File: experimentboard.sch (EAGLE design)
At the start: 72 parts, among them IC1 TL072P, IC2 LM317, IC3 LM337, Q1 27 MHz, U1 PCM1690, U2 PLL1706

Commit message: Taking the Beaglebone approach
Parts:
- removed C16, C17, C18: 100 nF ml, rcl:C-EU050-024X044
- removed Q1: 27 MHz, special:XTAL/S
- removed R2: 22, rcl:R-EU_0207/7
- removed SV1: (no value), 0000halfgaar:RASPBERRYPI2
- added JP1, JP2: (no value), jumper:JP2Q
- added R15: 680, rcl:R-EU_0207/7
- added R27: 0, rcl:R-EU_0207/10
- added R30, R31, R32, R33, R35, R36, R37: 22, rcl:R-EU_0207/7
- added R38, R39: 5.6k, rcl:R-EU_0207/7
- added U$2: BEAGLEBONEP9, 0000halfgaar:BEAGLEBONEP9
- C1: value 22pf -> 4.7n
- C15: value 100 nF ml -> 1µF ml
- C2: value 22pf -> 68n
- R1: value 22 -> 0; device rcl:R-EU_0207/7 -> rcl:R-EU_0207/10
- R23, R24: value 2.7k -> 715
- R3: value 22 -> 10k
- U2: value PLL1706 -> DIR9001; device 0000halfgaar:PLL1705 -> 0000halfgaar:DIR9001
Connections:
- removed net MOSI: SV1.GPIO10/MOSI, U1.MD/SDA/DEMP, U2.FS1/MD
- removed net N$10: R1.1, SV1.GPIO19/LRCK
- removed net N$9: R2.1, SV1.GPIO18/BCK
- removed net SCKL: SV1.GPIO11/SCLK, U1.MC/SCL/FMT, U2.FS2/MC
- removed net U1SEL: SV1.GPIO22, U1.MS/ADR0/RSV
- removed net U2SEL: SV1.GPIO15, U2.SR/ML
- new net ACLKR: R31.1, U$2.ACLKR
- new net ACLKX: R36.1, U$2.ACLKX
- new net AHCLKX: R35.1, U$2.FSX
- new net DIN: R32.1, U$2.DIN
- new net DIR_AUDIO: U$2.DIR_AUDIO(GPIO1_19), U2.AUDIO
- new net DOUT: R37.1, U$2.DOUT
- new net FSR: R30.1, U$2.FSR
- new net MCLK: R4.1, U$2.AHCLKX
- new net N$20: U2.RXIN
- new net N$51: R32.2, U2.DOUT
- new net N$52: R31.2, U2.BCKO
- new net N$53: R30.2, U2.LRCKO
- new net N$54: R33.2, U2.SCKO
- new net N$61: R37.2, U1.DIN1
- new net N$62: R36.2, U1.BCK
- new net N$63: R35.2, U1.LRCK
- new net RST: U$2.RESET(GPIO1_16), U1.RST, U2.RST
- new net SCL: R38.1, U$2.I2C_SCL, U1.MC/SCL/FMT
- new net SDA: R39.1, U$2.I2C_SDA, U1.MD/SDA/DEMP
- net AGND: now also C1.1, C2.1, R1.2; no longer C16.1
- net DGND: now also C15.2, R1.1, R7.1, U$2.DGND, U2.DGND, U2.RSV, U2.XTI; no longer C1.1, C15.1, C17.1, C18.2, C2.1, SV1.GND@1, U2.DGND1, U2.DGND2, U2.DGND3
- net N$1: now also JP2.3, U2.PSCK1; no longer R1.2, U1.LRCK
- net N$2: now also R3.2, U1.TEST/ADR1/RSV; no longer R2.2, U1.BCK
- net N$3: now also JP2.1, U2.PSCK0; no longer R3.2, U1.DIN1
- net N$4: now also C1.2, R15.1, U2.FILT; no longer R4.1, U2.SCKO3
- net N$6: now also C2.2, R15.2; no longer C1.2, Q1.2, U2.XT1
- net N$7: now also JP1.4, U2.FMT0; no longer C2.2, Q1.1, U2.XT2
- net N$8: now also JP1.2, U2.FMT1; no longer R3.1, SV1.GPIO21/I2SOUT
- net V+: now also R27.2
- net VCC: now also R27.1, U$2.VDD_5V; no longer C16.2
- net VDD: now also C15.1, JP1.1, JP1.3, JP2.2, JP2.4, R3.1, R38.2, R39.2, U$2.3.3V, U2.VDD; no longer C15.2, C17.2, C18.1, R7.1, SV1.3V3@1, SV1.3V3@2, U1.RST, U2.VDD1, U2.VDD2, U2.VDD3
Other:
- moved on the sheet: C1, C15, C2, C32, R1, R3, R4

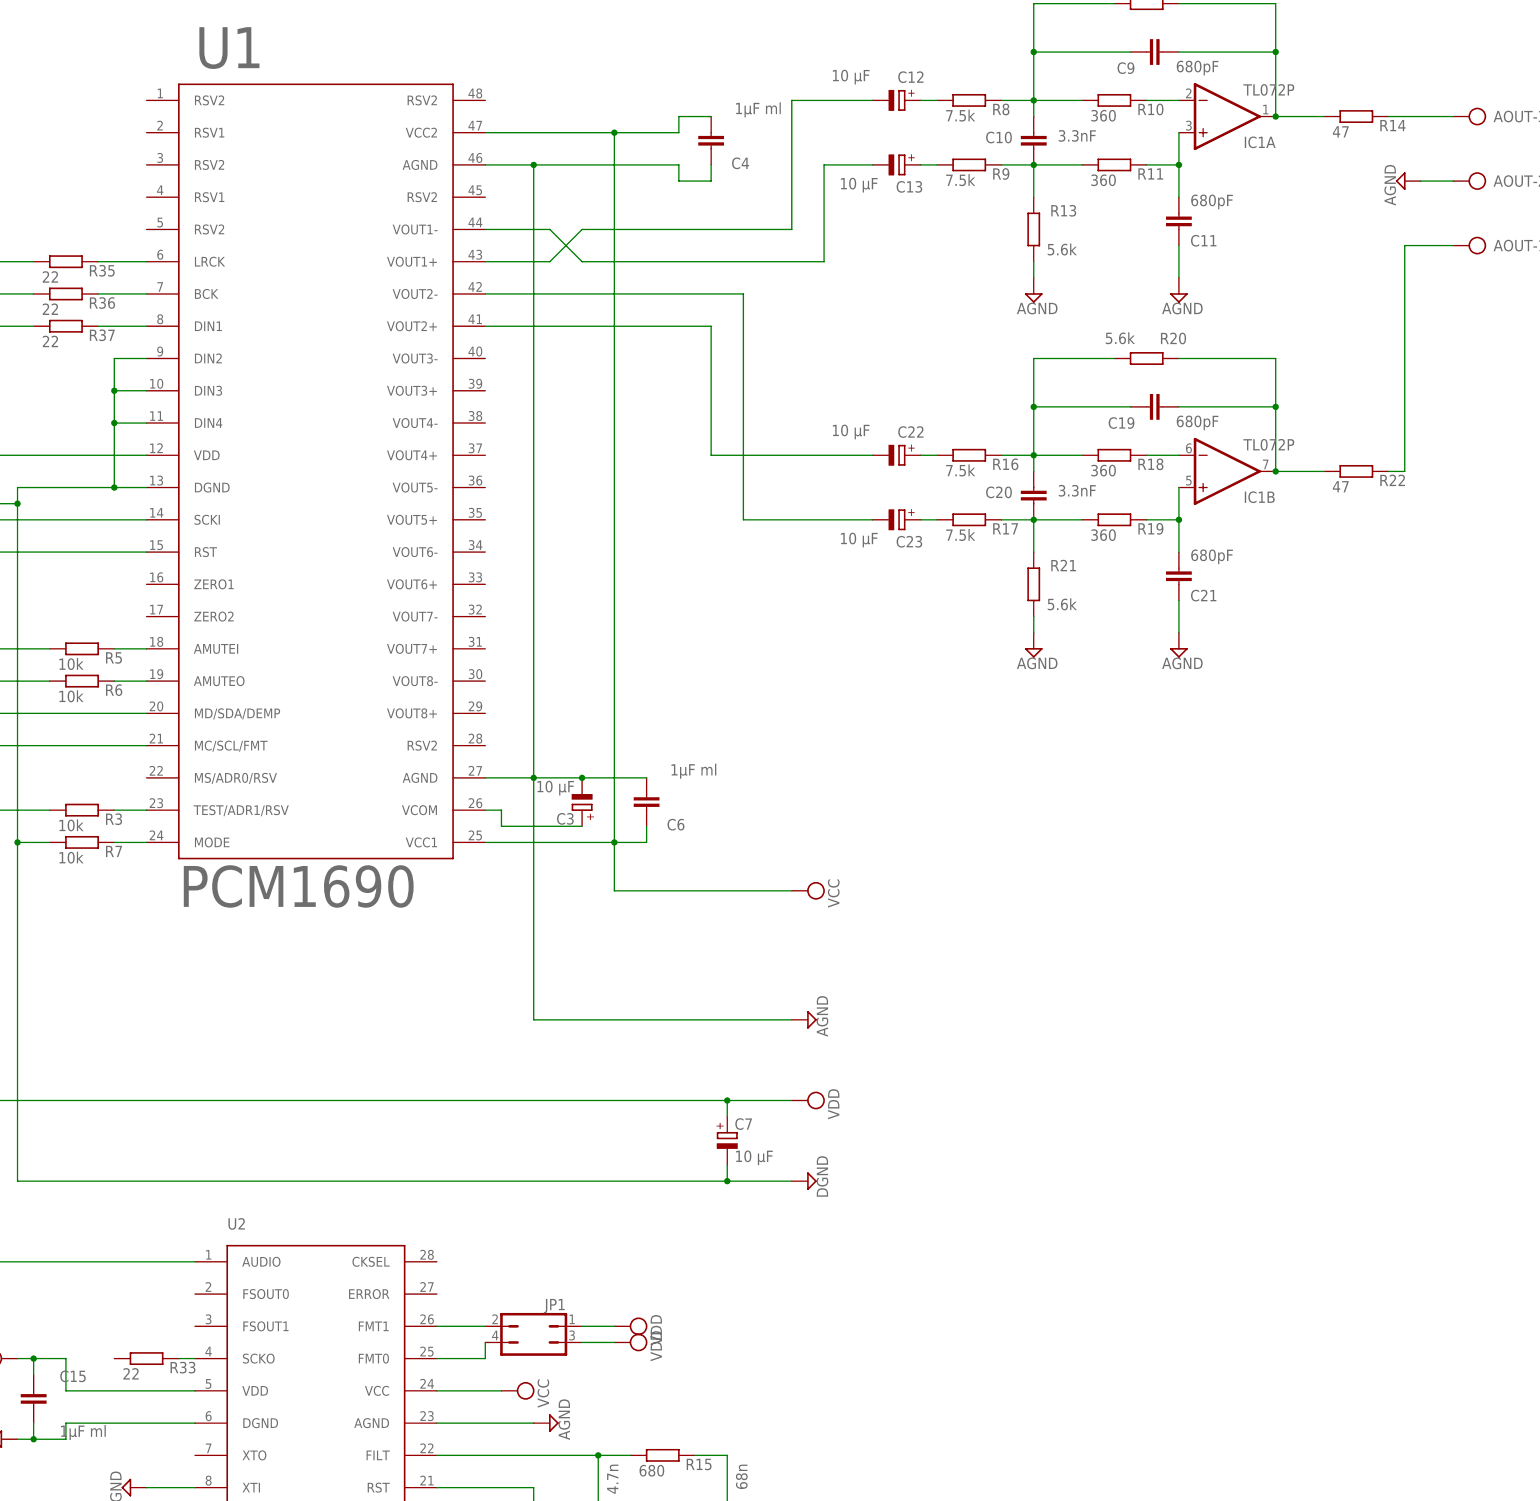
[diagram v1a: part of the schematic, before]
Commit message: Reversed opamp
Because signals are now on top layer, the layout had to be mirrored.
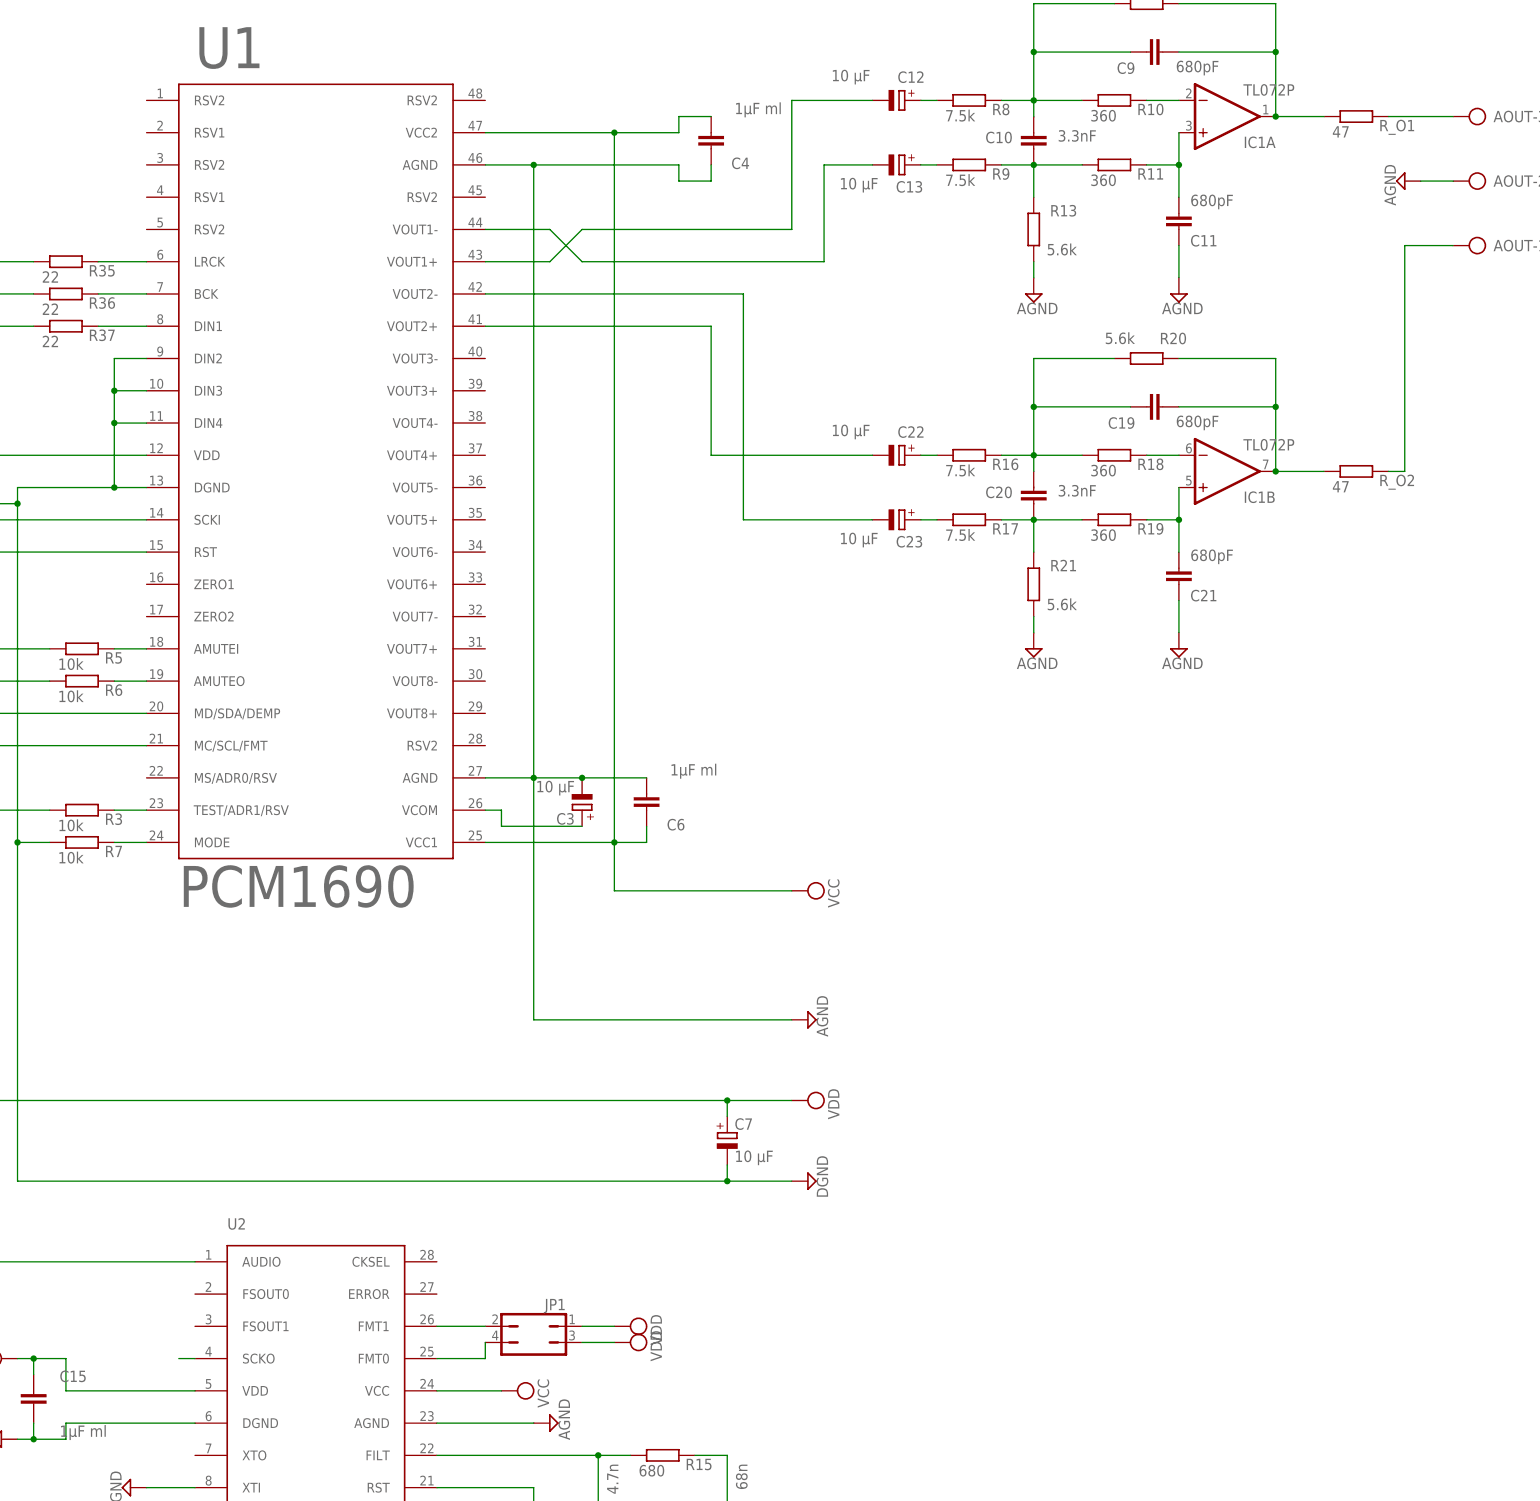
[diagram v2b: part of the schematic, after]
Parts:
- removed R33: 22, rcl:R-EU_0207/7
- renumbered R14 to R_O1, R22 to R_O2
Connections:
- net N$54: no longer R33.2
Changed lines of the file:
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@@
 <grid distance="0.1" unitdist="inch" unit="inch" style="lines" multiple="1" display="no" altdistance="0.01" altunitdist="inch" altunit="inch"/>
 <layers>
-<layer number="1" name="Top" color="4" fill="1" visible="yes" active="no"/>
-<layer number="2" name="Route2" color="1" fill="3" visible="yes" active="no"/>
-<layer number="3" name="Route3" color="4" fill="3" visible="yes" active="no"/>
-<layer number="14" name="Route14" color="1" fill="6" visible="yes" active="no"/>
-<layer number="15" name="Route15" color="4" fill="6" visible="yes" active="no"/>
-<layer number="16" name="Bottom" color="1" fill="1" visible="yes" active="no"/>
-<layer number="17" name="Pads" color="2" fill="1" visible="yes" active="no"/>
-<layer number="18" name="Vias" color="2" fill="1" visible="yes" active="no"/>
-<layer number="19" name="Unrouted" color="6" fill="1" visible="yes" active="no"/>
-<layer number="20" name="Dimension" color="15" fill="1" visible="yes" active="no"/>
-<layer number="21" name="tPlace" color="7" fill="1" visible="yes" active="no"/>
-<layer number="22" name="bPlace" color="7" fill="1" visible="yes" active="no"/>
-<layer number="23" name="tOrigins" color="15" fill="1" visible="yes" active="no"/>
-<layer number="24" name="bOrigins" color="15" fill="1" visible="yes" active="no"/>
-<layer number="25" name="tNames" color="7" fill="1" visible="yes" active="no"/>
-<layer number="26" name="bNames" color="7" fill="1" visible="yes" active="no"/>
-<layer number="27" name="tValues" color="7" fill="1" visible="yes" active="no"/>
-<layer number="28" name="bValues" color="7" fill="1" visible="yes" active="no"/>
+<layer number="1" name="Top" color="4" fill="1" visible="no" active="no"/>
+<layer number="2" name="Route2" color="1" fill="3" visible="no" active="no"/>
+<layer number="3" name="Route3" color="4" fill="3" visible="no" active="no"/>
+<layer number="14" name="Route14" color="1" fill="6" visible="no" active="no"/>
+<layer number="15" name="Route15" color="4" fill="6" visible="no" active="no"/>
+<layer number="16" name="Bottom" color="1" fill="1" visible="no" active="no"/>
+<layer number="17" name="Pads" color="2" fill="1" visible="no" active="no"/>
+<layer number="18" name="Vias" color="2" fill="1" visible="no" active="no"/>
+<layer number="19" name="Unrouted" color="6" fill="1" visible="no" active="no"/>
+<layer number="20" name="Dimension" color="15" fill="1" visible="no" active="no"/>
+<layer number="21" name="tPlace" color="7" fill="1" visible="no" active="no"/>
+<layer number="22" name="bPlace" color="7" fill="1" visible="no" active="no"/>
+<layer number="23" name="tOrigins" color="15" fill="1" visible="no" active="no"/>
+<layer number="24" name="bOrigins" color="15" fill="1" visible="no" active="no"/>
+<layer number="25" name="tNames" color="7" fill="1" visible="no" active="no"/>
+<layer number="26" name="bNames" color="7" fill="1" visible="no" active="no"/>
+<layer number="27" name="tValues" color="7" fill="1" visible="no" active="no"/>
+<layer number="28" name="bValues" color="7" fill="1" visible="no" active="no"/>
 <layer number="29" name="tStop" color="7" fill="3" visible="no" active="no"/>
 <layer number="30" name="bStop" color="7" fill="6" visible="no" active="no"/>
@@
 <layer number="35" name="tGlue" color="7" fill="4" visible="no" active="no"/>
 <layer number="36" name="bGlue" color="7" fill="5" visible="no" active="no"/>
-<layer number="37" name="tTest" color="7" fill="1" visible="yes" active="no"/>
-<layer number="38" name="bTest" color="7" fill="1" visible="yes" active="no"/>
+<layer number="37" name="tTest" color="7" fill="1" visible="no" active="no"/>
+<layer number="38" name="bTest" color="7" fill="1" visible="no" active="no"/>
 <layer number="39" name="tKeepout" color="4" fill="11" visible="no" active="no"/>
 <layer number="40" name="bKeepout" color="1" fill="11" visible="no" active="no"/>
@@
 <layer number="44" name="Drills" color="7" fill="1" visible="no" active="no"/>
 <layer number="45" name="Holes" color="7" fill="1" visible="no" active="no"/>
-<layer number="46" name="Milling" color="3" fill="1" visible="yes" active="no"/>
-<layer number="47" name="Measures" color="7" fill="1" visible="yes" active="no"/>
-<layer number="48" name="Document" color="7" fill="1" visible="yes" active="no"/>
-<layer number="49" name="Reference" color="7" fill="1" visible="yes" active="no"/>
-<layer number="51" name="tDocu" color="7" fill="1" visible="yes" active="no"/>
-<layer number="52" name="bDocu" color="7" fill="1" visible="yes" active="no"/>
+<layer number="46" name="Milling" color="3" fill="1" visible="no" active="no"/>
+<layer number="47" name="Measures" color="7" fill="1" visible="no" active="no"/>
+<layer number="48" name="Document" color="7" fill="1" visible="no" active="no"/>
+<layer number="49" name="Reference" color="7" fill="1" visible="no" active="no"/>
+<layer number="51" name="tDocu" color="7" fill="1" visible="no" active="no"/>
+<layer number="52" name="bDocu" color="7" fill="1" visible="no" active="no"/>
 <layer number="90" name="Modules" color="5" fill="1" visible="yes" active="yes"/>
 <layer number="91" name="Nets" color="2" fill="1" visible="yes" active="yes"/>
@@
 <part name="C12" library="rcl" deviceset="CPOL-EU" device="E1.8-4" value="10 µF"/>
 <part name="C13" library="rcl" deviceset="CPOL-EU" device="E1.8-4" value="10 µF"/>
-<part name="R14" library="rcl" deviceset="R-EU_" device="0207/7" value="47"/>
+<part name="R_O1" library="rcl" deviceset="R-EU_" device="0207/7" value="47"/>
 <part name="SUPPLY15" library="supply2" deviceset="DGND" device=""/>
 <part name="SUPPLY16" library="supply2" deviceset="AGND" device=""/>
@@
 <part name="C22" library="rcl" deviceset="CPOL-EU" device="E1.8-4" value="10 µF"/>
 <part name="C23" library="rcl" deviceset="CPOL-EU" device="E1.8-4" value="10 µF"/>
-<part name="R22" library="rcl" deviceset="R-EU_" device="0207/10" value="47"/>
+<part name="R_O2" library="rcl" deviceset="R-EU_" device="0207/10" value="47"/>
 <part name="SUPPLY23" library="supply2" deviceset="AGND" device=""/>
 <part name="IC2" library="v-reg" deviceset="LM317TS" device="" value="LM317"/>
@@
 <part name="R31" library="rcl" deviceset="R-EU_" device="0207/7" value="22"/>
 <part name="R32" library="rcl" deviceset="R-EU_" device="0207/7" value="22"/>
-<part name="R33" library="rcl" deviceset="R-EU_" device="0207/7" value="22"/>
 <part name="R3" library="rcl" deviceset="R-EU_" device="0207/7" value="10k"/>
 <part name="U$2" library="0000halfgaar" deviceset="BEAGLEBONEP9" device=""/>
@@
 <attribute name="VALUE" x="185.293" y="105.3846" size="1.778" layer="96"/>
 </instance>
-<instance part="R14" gate="G$1" x="266.7" y="116.84" smashed="yes">
+<instance part="R_O1" gate="G$1" x="266.7" y="116.84" smashed="yes">
 <attribute name="NAME" x="270.256" y="114.5286" size="1.778" layer="95"/>
 <attribute name="VALUE" x="262.89" y="113.538" size="1.778" layer="96"/>
@@
 <attribute name="VALUE" x="185.293" y="49.5046" size="1.778" layer="96"/>
 </instance>
-<instance part="R22" gate="G$1" x="266.7" y="60.96" smashed="yes">
+<instance part="R_O2" gate="G$1" x="266.7" y="60.96" smashed="yes">
 <attribute name="NAME" x="270.256" y="58.6486" size="1.778" layer="95"/>
 <attribute name="VALUE" x="262.89" y="57.658" size="1.778" layer="96"/>
@@
 <attribute name="NAME" x="77.216" y="-121.6914" size="1.778" layer="95"/>
 <attribute name="VALUE" x="69.85" y="-122.682" size="1.778" layer="96"/>
-</instance>
-<instance part="R33" gate="G$1" x="76.2" y="-78.74" smashed="yes">
-<attribute name="NAME" x="79.756" y="-81.0514" size="1.778" layer="95"/>
-<attribute name="VALUE" x="72.39" y="-82.042" size="1.778" layer="96"/>
 </instance>
 <instance part="R3" gate="G$1" x="66.04" y="7.62" smashed="yes">
@@
 <wire x1="254" y1="116.84" x2="254" y2="127" width="0.1524" layer="91"/>
 <junction x="254" y="127"/>
-<pinref part="R14" gate="G$1" pin="1"/>
+<pinref part="R_O1" gate="G$1" pin="1"/>
 <wire x1="261.62" y1="116.84" x2="254" y2="116.84" width="0.1524" layer="91"/>
 <junction x="254" y="116.84"/>
@@
 <wire x1="254" y1="60.96" x2="254" y2="71.12" width="0.1524" layer="91"/>
 <junction x="254" y="71.12"/>
-<pinref part="R22" gate="G$1" pin="1"/>
+<pinref part="R_O2" gate="G$1" pin="1"/>
 <wire x1="261.62" y1="60.96" x2="254" y2="60.96" width="0.1524" layer="91"/>
 <pinref part="IC1" gate="B" pin="OUT"/>
@@
 <net name="N$37" class="0">
 <segment>
-<pinref part="R14" gate="G$1" pin="2"/>
+<pinref part="R_O1" gate="G$1" pin="2"/>
 <pinref part="AOUT" gate="-3" pin="KL"/>
 <wire x1="271.78" y1="116.84" x2="281.94" y2="116.84" width="0.1524" layer="91"/>
@@
 <net name="N$38" class="0">
 <segment>
-<pinref part="R22" gate="G$1" pin="2"/>
+<pinref part="R_O2" gate="G$1" pin="2"/>
 <wire x1="271.78" y1="60.96" x2="274.32" y2="60.96" width="0.1524" layer="91"/>
 <wire x1="274.32" y1="60.96" x2="274.32" y2="96.52" width="0.1524" layer="91"/>
@@
 <segment>
 <pinref part="U2" gate="G$1" pin="SCKO"/>
-<pinref part="R33" gate="G$1" pin="2"/>
 <wire x1="83.82" y1="-78.74" x2="81.28" y2="-78.74" width="0.1524" layer="91"/>
 </segment>
